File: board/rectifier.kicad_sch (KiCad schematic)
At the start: 2 parts

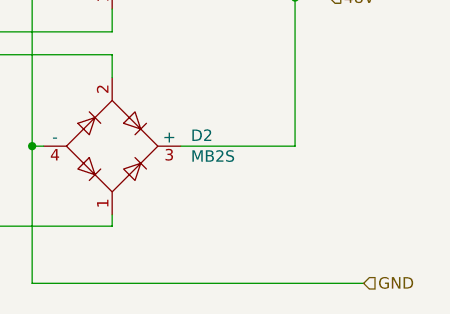
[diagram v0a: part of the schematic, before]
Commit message: updated to v1.0 of put_on_edge
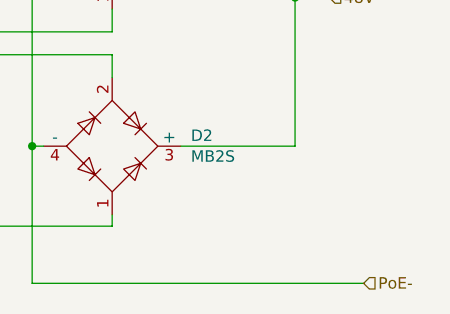
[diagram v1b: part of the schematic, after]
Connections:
- net GND renamed PoE-
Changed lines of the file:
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@@
     (effects (font (size 1.27 1.27)) (justify left))
   )
-  (hierarchical_label "GND" (shape input) (at 156.21 149.86 0)
+  (hierarchical_label "PoE-" (shape input) (at 156.21 149.86 0)
     (effects (font (size 1.27 1.27)) (justify left))
   )
